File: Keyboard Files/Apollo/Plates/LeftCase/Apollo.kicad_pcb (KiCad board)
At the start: 2 copper layers, 166.1 x 133.7 mm, 37 parts

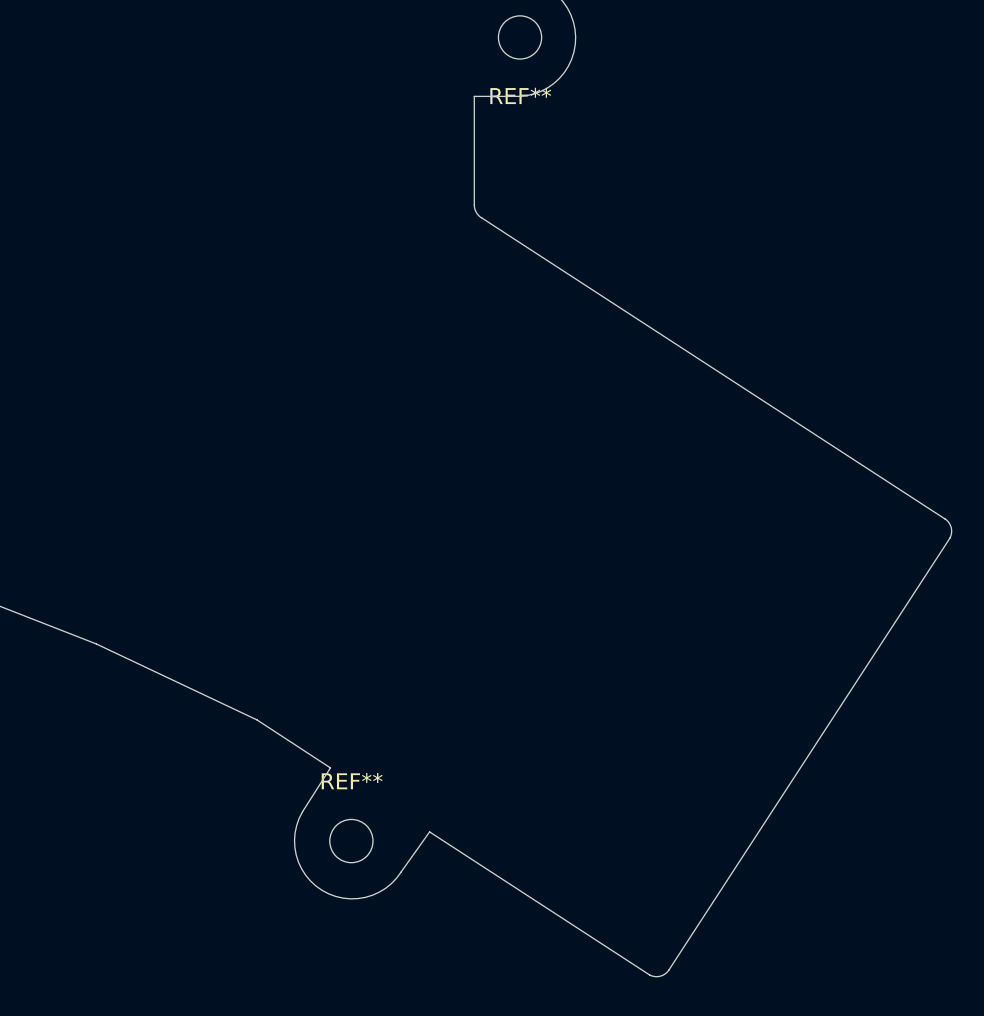
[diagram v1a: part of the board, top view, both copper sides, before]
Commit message: Redo thumb keys plates
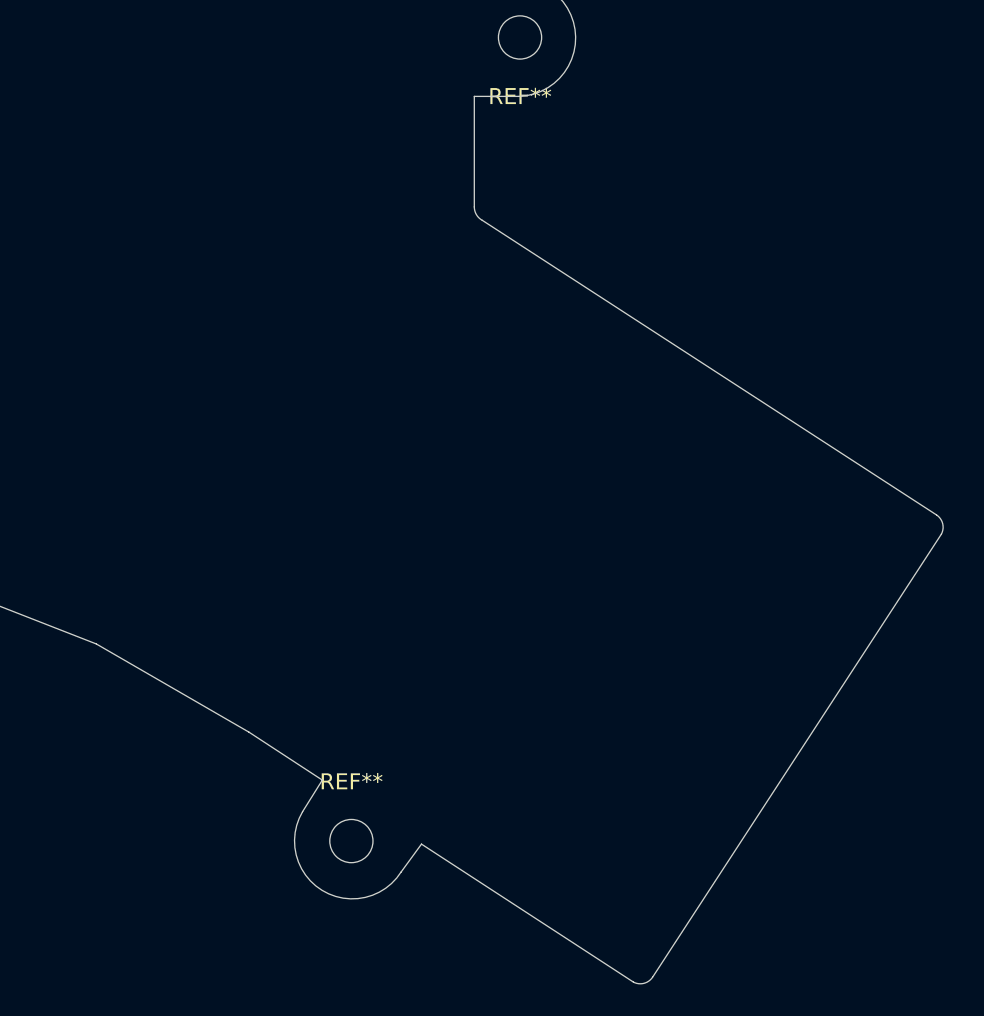
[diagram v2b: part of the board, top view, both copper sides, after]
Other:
- board size 166.1 x 133.7 mm -> 165.6 x 134.1 mm
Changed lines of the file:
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@@
   (gr_line (start 69.849003 60.449135) (end 69.85 63.119) (layer Edge.Cuts) (width 0.05))
   (gr_line (start 53.5305 124.3965) (end 56.3245 124.3965) (layer Edge.Cuts) (width 0.05))
-  (gr_line (start 177.2539 175.0695) (end 172.6692 172.0723) (layer Edge.Cuts) (width 0.05))
-  (gr_line (start 162.6235 167.3225) (end 172.6692 172.0723) (layer Edge.Cuts) (width 0.05))
-  (gr_line (start 177.2539 175.0695) (end 175.514 177.8) (layer Edge.Cuts) (width 0.05))
-  (gr_line (start 183.4515 179.07) (end 181.667224 181.579386) (layer Edge.Cuts) (width 0.05))
+  (gr_line (start 176.7459 175.8315) (end 172.1612 172.8343) (layer Edge.Cuts) (width 0.05))
+  (gr_line (start 162.6235 167.3225) (end 172.1612 172.8343) (layer Edge.Cuts) (width 0.05))
+  (gr_line (start 176.7459 175.8315) (end 175.514 177.8) (layer Edge.Cuts) (width 0.05))
+  (gr_line (start 182.9435 179.832) (end 181.667224 181.579386) (layer Edge.Cuts) (width 0.05))
   (gr_arc (start 178.6188 179.6438) (end 175.514 177.8) (angle -178.2907958) (layer Edge.Cuts) (width 0.05))
   (gr_line (start 186.246182 60.7695) (end 186.2455 125.7935) (layer Edge.Cuts) (width 0.05))
@@
   (gr_line (start 53.654635 131.699997) (end 56.3245 131.699) (layer Edge.Cuts) (width 0.05))
   (gr_arc (start 53.6425 128.0474) (end 53.5305 124.3965) (angle -178.4332201) (layer Edge.Cuts) (width 0.05))
-  (gr_line (start 183.4515 179.07) (end 197.2056 188.0108) (layer Edge.Cuts) (width 0.05))
-  (gr_line (start 186.2455 133.096) (end 186.2455 139.877351) (layer Edge.Cuts) (width 0.05))
+  (gr_line (start 182.9435 179.832) (end 196.1896 188.4553) (layer Edge.Cuts) (width 0.05))
+  (gr_line (start 186.2455 133.096) (end 186.2455 140.004351) (layer Edge.Cuts) (width 0.05))
   (gr_line (start 69.85 63.119) (end 57.7215 63.119) (layer Edge.Cuts) (width 0.05))
   (gr_line (start 56.3245 131.699) (end 56.3245 163.068) (layer Edge.Cuts) (width 0.05))
   (gr_line (start 112.457818 159.7025) (end 110.363 159.7025) (layer Edge.Cuts) (width 0.05))
-  (gr_arc (start 187.198 139.877351) (end 186.2455 139.877351) (angle -61.69924423) (layer Edge.Cuts) (width 0.05))
-  (gr_arc (start 215.160868 160.274001) (end 215.973667 160.7058) (angle -84.28945016) (layer Edge.Cuts) (width 0.05))
-  (gr_line (start 186.74642 140.716) (end 215.6714 159.512) (layer Edge.Cuts) (width 0.05))
-  (gr_arc (start 197.637399 187.198001) (end 197.2056 188.0108) (angle -84.28945016) (layer Edge.Cuts) (width 0.05))
-  (gr_line (start 215.973667 160.7058) (end 198.403199 187.708533) (layer Edge.Cuts) (width 0.05))
+  (gr_arc (start 187.198 140.004351) (end 186.2455 140.004351) (angle -61.69924423) (layer Edge.Cuts) (width 0.05))
+  (gr_arc (start 214.627468 160.0238) (end 215.440267 160.455599) (angle -84.28945016) (layer Edge.Cuts) (width 0.05))
+  (gr_line (start 186.74642 140.843) (end 215.138 159.258) (layer Edge.Cuts) (width 0.05))
+  (gr_arc (start 196.621399 187.642501) (end 196.1896 188.4553) (angle -84.28945016) (layer Edge.Cuts) (width 0.05))
+  (gr_line (start 215.440267 160.455599) (end 197.387199 188.153033) (layer Edge.Cuts) (width 0.05))
   (gr_line (start 144.907 160.401) (end 162.6235 167.3225) (layer Edge.Cuts) (width 0.05))
   (gr_line (start 126.873 159.7025) (end 144.907 160.401) (layer Edge.Cuts) (width 0.05))
